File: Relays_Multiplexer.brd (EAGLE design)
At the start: 160 x 100 mm, 89 parts, among them IC1 PCA9685, IC2 PCA9685, J1 PTH VERT MALE, J2 1x33 Molex Connector, J3 PTH VERT FEMALE, J4 PTH VERT FEMALE, J5 2x17 PTH RA FEMALE

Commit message: Killed routes >:) and rearranged board
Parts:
- moved J5 123.0 mm to (99.1, 76.2), turned to 90 degrees
- moved J4 94.1 mm to (6.35, 78.7), turned to 270 degrees
- moved J2 92.7 mm to (7.62, 88.9), turned to 270 degrees
- moved J3 80.1 mm to (6.35, 68.6), turned to 270 degrees
- moved J1 34.3 mm to (6.35, 57.1), turned to 270 degrees
- moved RELAY22 26.9 mm to (25.4, 74.9)
- moved RELAY23 25.2 mm to (25.4, 69.8)
- moved RELAY24 20.4 mm to (25.4, 64.8)
- moved R36 14.2 mm to (17.8, 68.6)
- moved RELAY25 14.0 mm to (25.4, 59.7)
- moved RELAY21 13.5 mm to (25.4, 80.0)
- moved RELAY20 12.0 mm to (25.4, 85.1)
- moved R41 12.0 mm to (27.9, 53.3)
- moved R35 11.7 mm to (17.8, 78.7)
- moved RELAY19 10.9 mm to (25.4, 90.2)
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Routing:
- net N$10: track 9.48 -> 0.00 mm
- net N$9: track 7.01 -> 0.00 mm
- net N$8: track 5.31 -> 0.00 mm
- net N$109: track 4.15 -> 0.00 mm
- net N$108: track 4.15 -> 0.00 mm
- net N$110: track 3.63 -> 0.00 mm
- net N$107: track 3.63 -> 0.00 mm
- net N$106: track 3.63 -> 0.00 mm
- net N$105: track 3.63 -> 0.00 mm
- net N$7: track 3.28 -> 0.00 mm
- net N$104: track 3.10 -> 0.00 mm
- net N$103: track 3.10 -> 0.00 mm

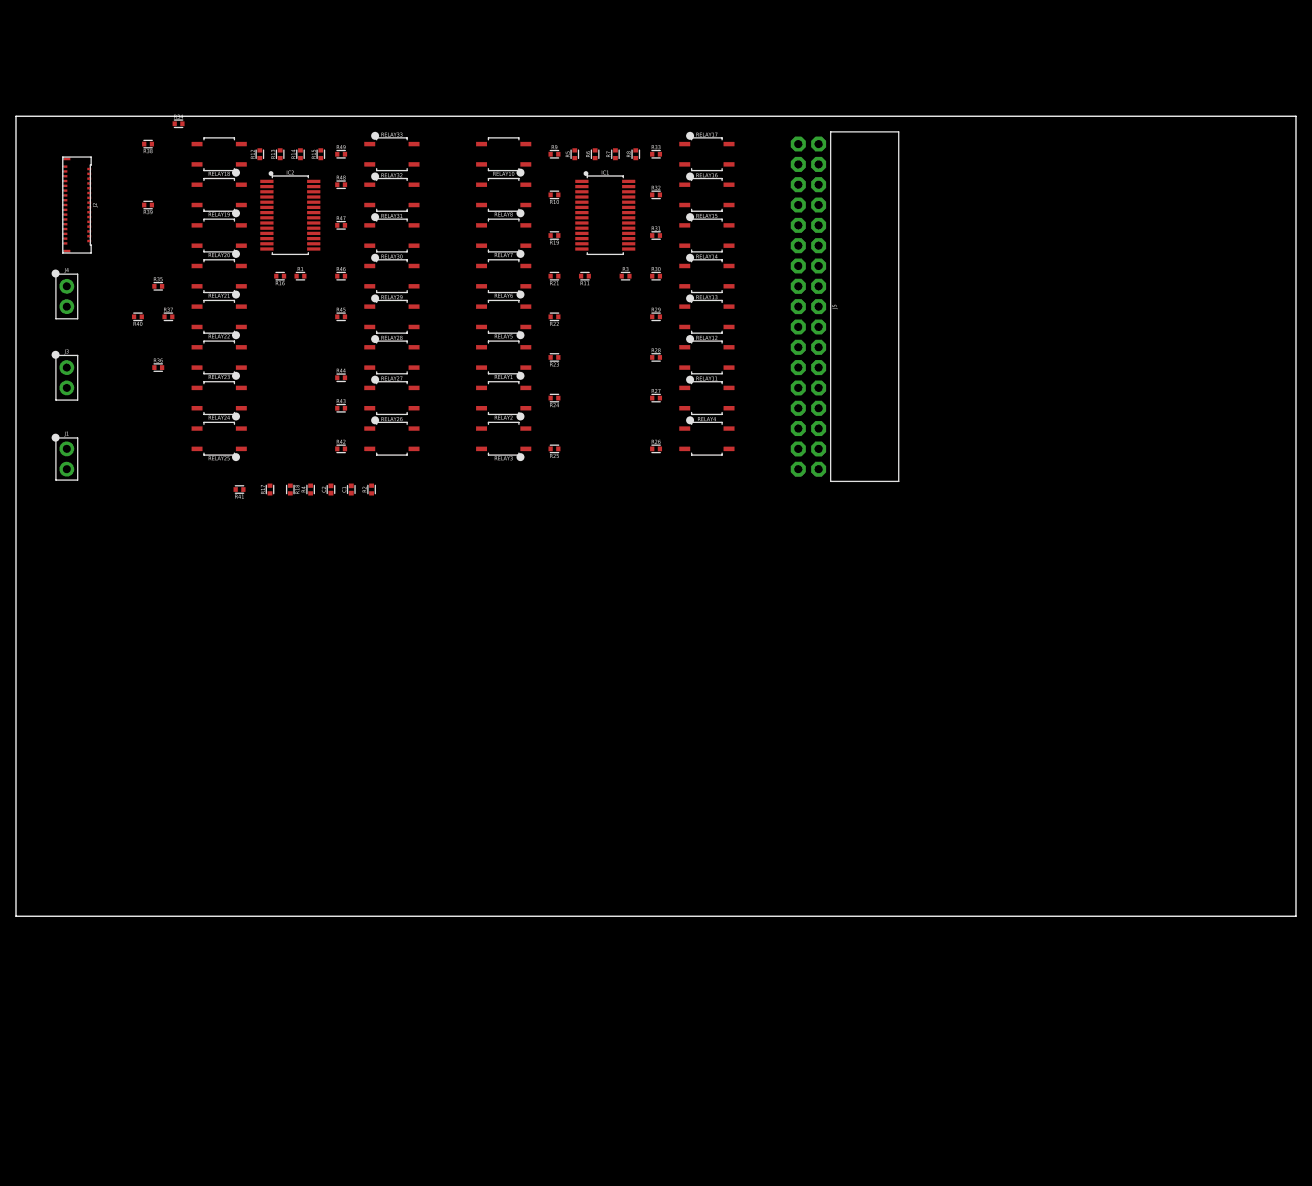
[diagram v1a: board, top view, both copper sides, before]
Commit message: Board is fully routed, but kind of looks like shit
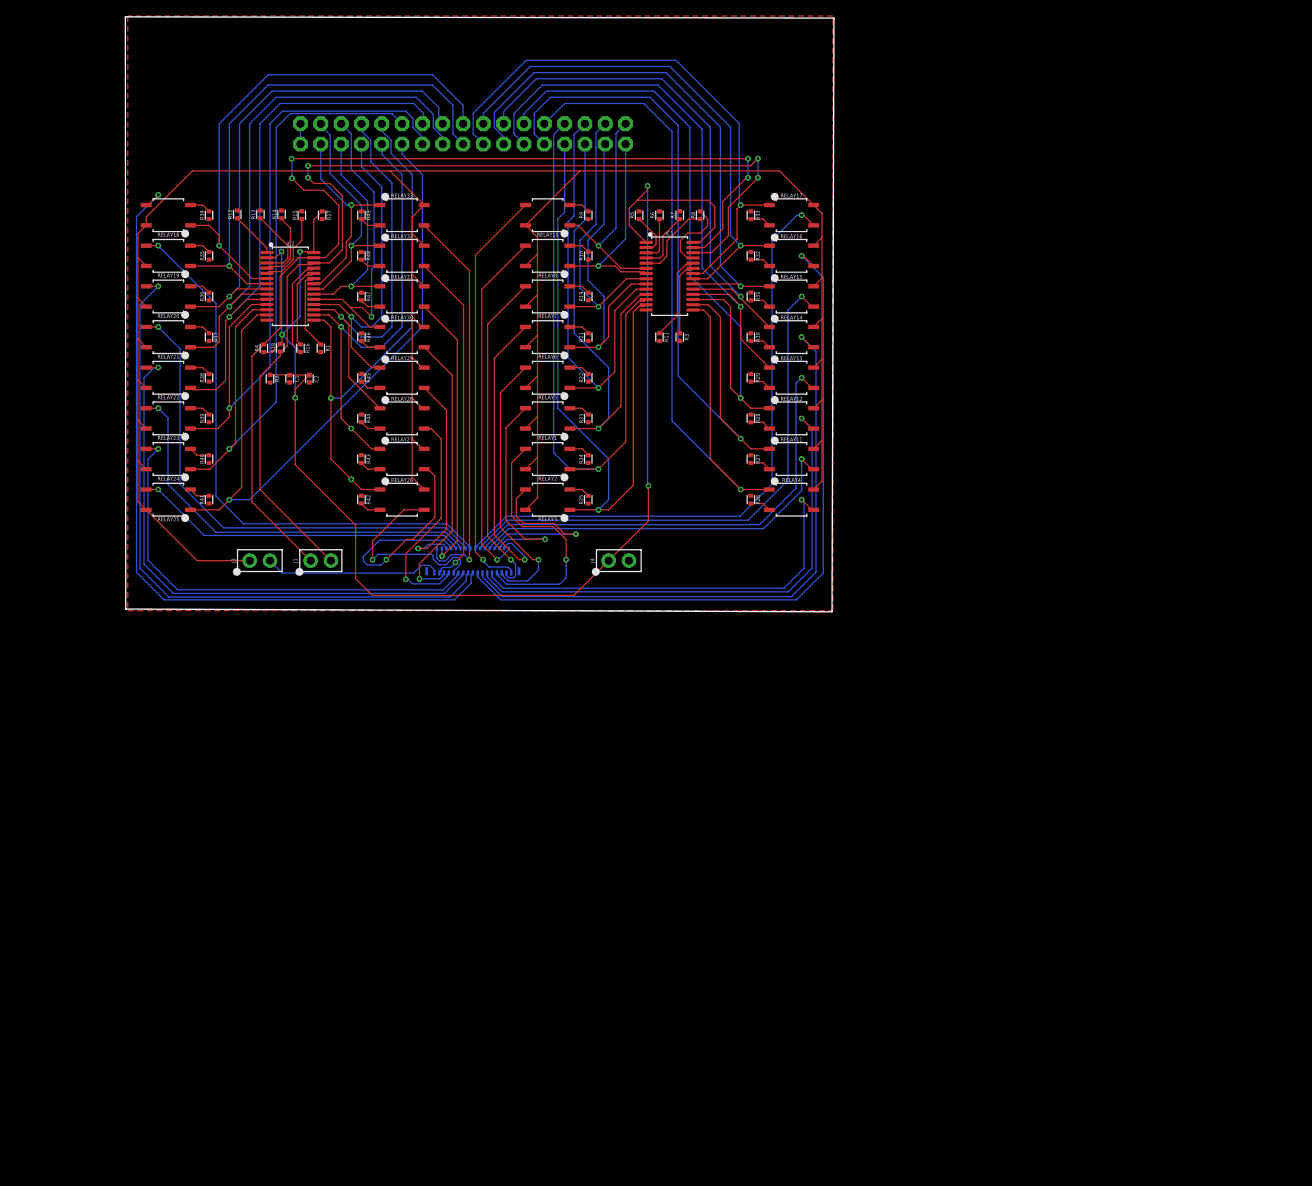
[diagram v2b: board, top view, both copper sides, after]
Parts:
- moved J4 75.9 mm to (74.1, 44.5), turned to 0 degrees
- moved J2 66.5 mm to (57.1, 44.5), flipped to the bottom, turned to 0 degrees
- moved J5 48.3 mm to (55.9, 97.8), flipped to the bottom, turned to 180 degrees
- moved R17 34.9 mm to (38.3, 87.6), turned to 270 degrees
- moved J1 34.2 mm to (38.1, 44.5), turned to 0 degrees
- moved J3 33.2 mm to (29.2, 44.5), turned to 0 degrees
- moved R38 30.2 mm to (24.1, 67.3), turned to 90 degrees
- moved R39 27.7 mm to (24.1, 62.2), turned to 90 degrees
- moved R40 19.9 mm to (24.1, 57.1), turned to 90 degrees
- moved R2 18.8 mm to (31.8, 67.2), turned to 270 degrees
- moved R4 18.6 mm to (31.0, 71.0)
- moved R18 17.8 mm to (33.0, 71.0), turned to 90 degrees
- moved C1 15.8 mm to (34.2, 67.2), turned to 270 degrees
- moved C2 14.1 mm to (36.7, 67.2), turned to 270 degrees
- moved R29 14.1 mm to (91.9, 67.3), turned to 270 degrees
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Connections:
- net SW12 renamed SW
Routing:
- net AVCC: track 0.00 -> 309.0 mm
- net VCC: track 0.00 -> 186.0 mm, vias 0 -> 6
- net N$13: track 0.00 -> 135.6 mm, vias 0 -> 4
- net N$14: track 0.00 -> 135.5 mm, vias 0 -> 4
- net SW9: track 0.00 -> 96.0 mm, vias 0 -> 1
- net N$17: track 0.00 -> 95.8 mm, vias 0 -> 1
- net SW10: track 0.00 -> 91.5 mm, vias 0 -> 1
- net N$19: track 0.00 -> 89.1 mm, vias 0 -> 1
- net SW24: track 0.00 -> 88.1 mm, vias 0 -> 1
- net SW23: track 0.00 -> 86.0 mm, vias 0 -> 1
- net SW22: track 0.00 -> 82.8 mm, vias 0 -> 1
- net SW11: track 0.00 -> 82.7 mm, vias 0 -> 1
- net SW8: track 0.00 -> 82.1 mm, vias 0 -> 1
- net N$35: track 0.00 -> 81.9 mm, vias 0 -> 1
- net N$18: track 0.00 -> 78.0 mm, vias 0 -> 1
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- added copper zone on layer 1, net GND
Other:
- board size 160 x 100 mm -> 88.6 x 74.4 mm

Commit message: Board is fully routed. We out here finishing things
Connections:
- net N$13 renamed SDA
- net N$14 renamed SCL
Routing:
- added copper zone on layer 16, net GND
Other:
- board size 88.6 x 74.4 mm -> 87.2 x 68.6 mm
- board text added: "+5V"
- board text added: "GND"
- board text added: "SCL"
- board text added: "SDA"
- board text added: "SW1"
- board text added: "SW2"
- board text added: "Sig +"
- board text added: "Sig -"

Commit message: Board is fully routed. We out here finishing things part 2
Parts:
- J1: value PTH VERT MALE -> PTH VERT FEMALE; device _connectors:HDRV2W64P254_1X2_508X254X838B -> _connectors:HDRVR2W64P254_1X2_558X254X850B
- moved J1 0.55 mm to (37.5, 44.5)
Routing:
- net SDA: track 135.6 -> 136.2 mm
- net SCL: track 135.5 -> 136.2 mm
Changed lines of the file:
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@@
 <text x="28.45" y="42.65" size="1" layer="21" font="vector" ratio="10" rot="R270">Sig +</text>
 <text x="30.9" y="42.6" size="1" layer="21" font="vector" ratio="10" rot="R270">Sig -</text>
-<text x="36.1" y="42.55" size="1" layer="21" font="vector" ratio="10" rot="R270">SDA</text>
-<text x="38.9" y="42.5" size="1" layer="21" font="vector" ratio="10" rot="R270">SCL</text>
+<text x="37.05" y="42.6" size="1" layer="21" font="vector" ratio="10" rot="R270">SDA</text>
+<text x="39.8" y="42.55" size="1" layer="21" font="vector" ratio="10" rot="R270">SCL</text>
 <text x="73.5" y="42.3" size="1" layer="21" font="vector" ratio="10" rot="R270">+5V</text>
 <text x="76.1" y="42.35" size="1" layer="21" font="vector" ratio="10" rot="R270">GND</text>
@@
 <attribute name="VALUE" x="34.29" y="73.66" size="0.25" layer="27" font="vector" ratio="10" align="top-center"/>
 </element>
-<element name="J1" library="_connectors" package="HDRV2W64P254_1X2_508X254X838B" package3d_urn="urn:adsk.eagle:package:4781708/8" value="PTH VERT MALE" x="38.1" y="44.45" smashed="yes">
-<attribute name="DATASHEET" value="https://drawings-pdf.s3.amazonaws.com/C10436.pdf" x="77.47" y="-8.89" size="1.778" layer="27" display="off"/>
-<attribute name="DIST" value="Digikey" x="77.47" y="-8.89" size="1.778" layer="27" display="off"/>
-<attribute name="DISTLINK" value="https://www.digikey.com/products/en?keywords=S1012E-02-ND" x="77.47" y="-8.89" size="1.778" layer="27" display="off"/>
-<attribute name="DISTPN" value="S1012E-02-ND" x="77.47" y="-8.89" size="1.778" layer="27" display="off"/>
-<attribute name="MFR" value="Sullins Connector Solutions" x="77.47" y="-8.89" size="1.778" layer="27" display="off"/>
-<attribute name="MPN" value="PEC02SAAN" x="77.47" y="-8.89" size="1.778" layer="27" display="off"/>
-<attribute name="NAME" x="35.179" y="44.45" size="0.5" layer="25" font="vector" ratio="10" rot="R90" align="bottom-center"/>
-<attribute name="VALUE" x="41.021" y="44.45" size="0.25" layer="27" font="vector" ratio="10" rot="R90" align="top-center"/>
+<element name="J1" library="_connectors" package="HDRVR2W64P254_1X2_558X254X850B" package3d_urn="urn:adsk.eagle:package:4781720/1" value="PTH VERT FEMALE" x="37.55" y="44.45" smashed="yes">
+<attribute name="DATASHEET" value="https://drawings-pdf.s3.amazonaws.com/10492.pdf" x="76.92" y="-8.89" size="1.778" layer="27" display="off"/>
+<attribute name="DIST" value="Digikey" x="76.92" y="-8.89" size="1.778" layer="27" display="off"/>
+<attribute name="DISTLINK" value="https://www.digikey.com/products/en?keywords=PPTC021LFBN-RC" x="76.92" y="-8.89" size="1.778" layer="27" display="off"/>
+<attribute name="DISTPN" value="S7000-ND" x="76.92" y="-8.89" size="1.778" layer="27" display="off"/>
+<attribute name="MFR" value="Sullins Connector Solutions" x="76.92" y="-8.89" size="1.778" layer="27" display="off"/>
+<attribute name="MPN" value="PPTC021LFBN-RC" x="76.92" y="-8.89" size="1.778" layer="27" display="off"/>
+<attribute name="NAME" x="35.629" y="44.45" size="0.5" layer="25" font="vector" ratio="10" rot="R90" align="bottom-center"/>
+<attribute name="VALUE" value="PTH VERT FEMALE" x="40.471" y="44.45" size="0.25" layer="27" font="vector" ratio="10" rot="R90" align="top-center"/>
 </element>
 <element name="R1" library="_resistors" package="RESC1005X35_SMD-0402" package3d_urn="urn:adsk.eagle:package:2899165/1" value="10K" x="38.1" y="71" smashed="yes" rot="R270">
@@
 <wire x1="33.31136875" y1="80.2782" x2="35.2044" y2="82.17123125" width="0.1524" layer="1"/>
 <wire x1="30.98" y1="71.4825" x2="29.5" y2="70.0025" width="0.1524" layer="1"/>
-<wire x1="29.5" y1="51.78" x2="36.83" y2="44.45" width="0.1524" layer="1"/>
-<wire x1="29.5" y1="70.0025" x2="29.5" y2="51.78" width="0.1524" layer="1"/>
+<wire x1="29.5" y1="51.311221875" x2="37.55" y2="44.45" width="0.1524" layer="1"/>
+<wire x1="29.5" y1="70.0025" x2="29.5" y2="51.311221875" width="0.1524" layer="1"/>
 <via x="91.5" y="92.3" extent="1-16" drill="0.254"/>
 <wire x1="84.6258" y1="83.585" x2="86.035" y2="83.585" width="0.1524" layer="1"/>
@@
 <contactref element="IC1" pad="26"/>
 <contactref element="IC2" pad="26"/>
-<wire x1="30.5" y1="53.32" x2="30.5" y2="67.5" width="0.1524" layer="1"/>
-<wire x1="30.5" y1="53.32" x2="39.37" y2="44.45" width="0.1524" layer="1"/>
+<wire x1="30.5" y1="52.838884375" x2="30.5" y2="67.5" width="0.1524" layer="1"/>
+<wire x1="30.5" y1="52.838884375" x2="40.09" y2="44.45" width="0.1524" layer="1"/>
 <wire x1="30.5" y1="67.5" x2="33.03" y2="70.03" width="0.1524" layer="1"/>
 <wire x1="33.03" y1="70.03" x2="33.03" y2="70.5675" width="0.1524" layer="1"/>

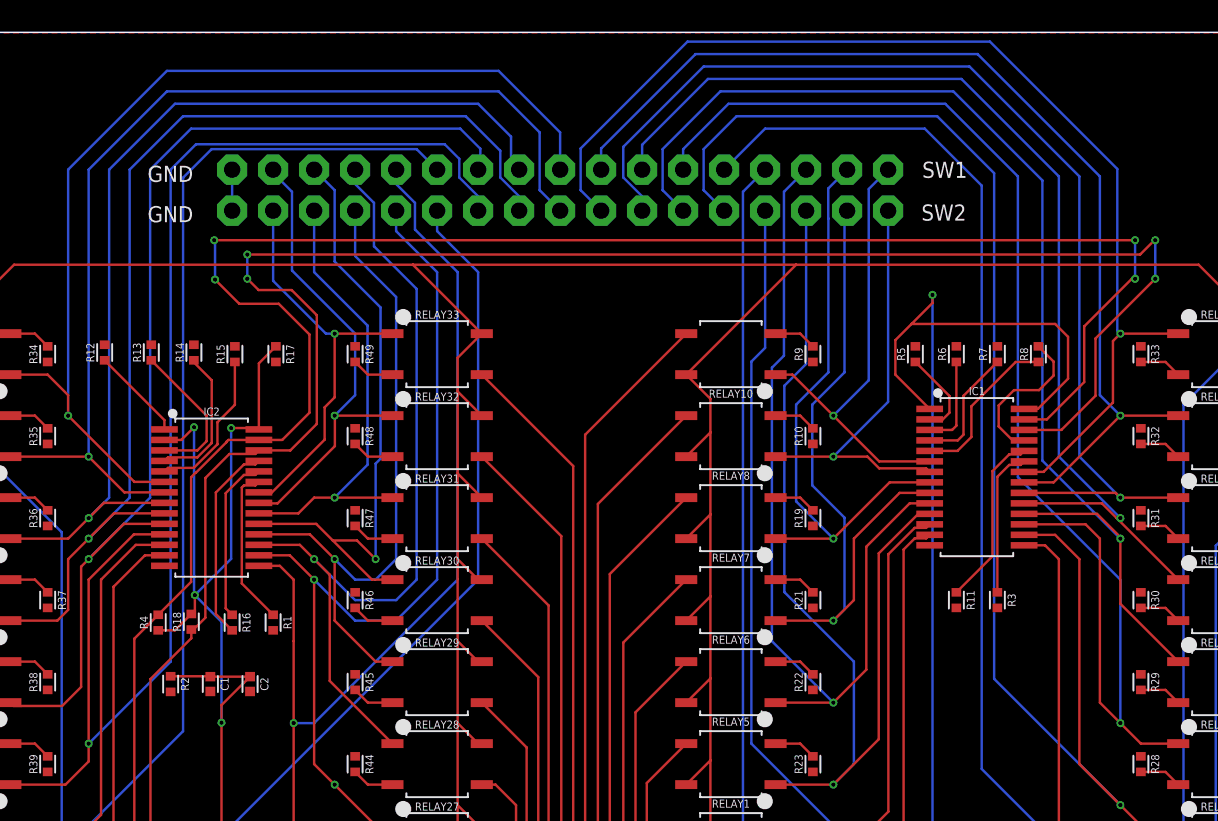
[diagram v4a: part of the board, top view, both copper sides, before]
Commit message: Updated some of the VCC connections.
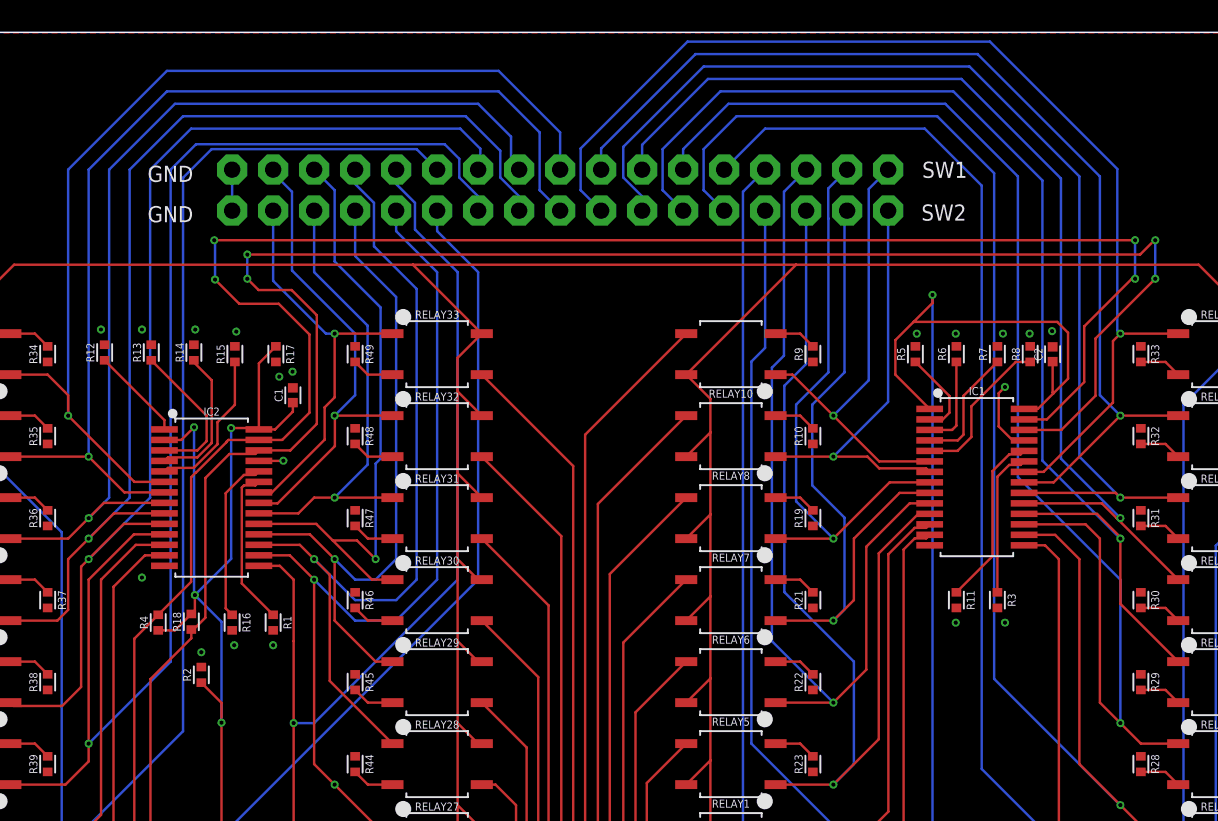
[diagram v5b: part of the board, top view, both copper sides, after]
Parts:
- moved C2 53.8 mm to (86.4, 87.6), turned to 90 degrees
- moved C1 18.6 mm to (39.3, 85.1), turned to 90 degrees
- moved R2 1.98 mm to (33.6, 67.8), turned to 90 degrees
- moved R8 0.51 mm to (85.0, 87.6)
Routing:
- net GND: track 24.6 -> 8.61 mm, vias 0 -> 19
- net N$4: track 10.1 -> 9.62 mm

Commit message: Added art and flexes
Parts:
- added U$1: (no value), _logo:LRG-LOGO
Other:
- board text added: "Designed by: Kristan Hilby"
- board text added: "Multiplexing Relay Board"
- board text added: "Rev. 1"
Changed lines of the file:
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@@
 <?xml version="1.0" encoding="utf-8"?>
 <!DOCTYPE eagle SYSTEM "eagle.dtd">
-<eagle version="9.3.1">
+<eagle version="9.3.0">
 <drawing>
 <settings>
@@
 <text x="81.1" y="99.55" size="1" layer="21" font="vector" ratio="10" rot="R180">SW1</text>
 <text x="81.05" y="96.9" size="1" layer="21" font="vector" ratio="10" rot="R180">SW2</text>
+<text x="15.2" y="105.75" size="1" layer="21" font="vector" ratio="15">Rev. 1</text>
+<text x="15.25" y="104.05" size="1" layer="21" font="vector" ratio="15">Multiplexing Relay Board</text>
+<text x="15.35" y="93.3" size="1" layer="21" font="vector" ratio="15">Designed by: Kristan Hilby</text>
 </plain>
 <attributes>
@@
 <attribute name="VALUE" x="55.88" y="101.79" size="0.25" layer="28" font="vector" ratio="10" rot="MR180" align="top-center"/>
 </element>
+<element name="U$1" library="_logo" package="LRG-LOGO" value="" x="22.65" y="99.15" smashed="yes"/>
 </elements>
 <signals>
